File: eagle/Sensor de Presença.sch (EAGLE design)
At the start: 4 parts

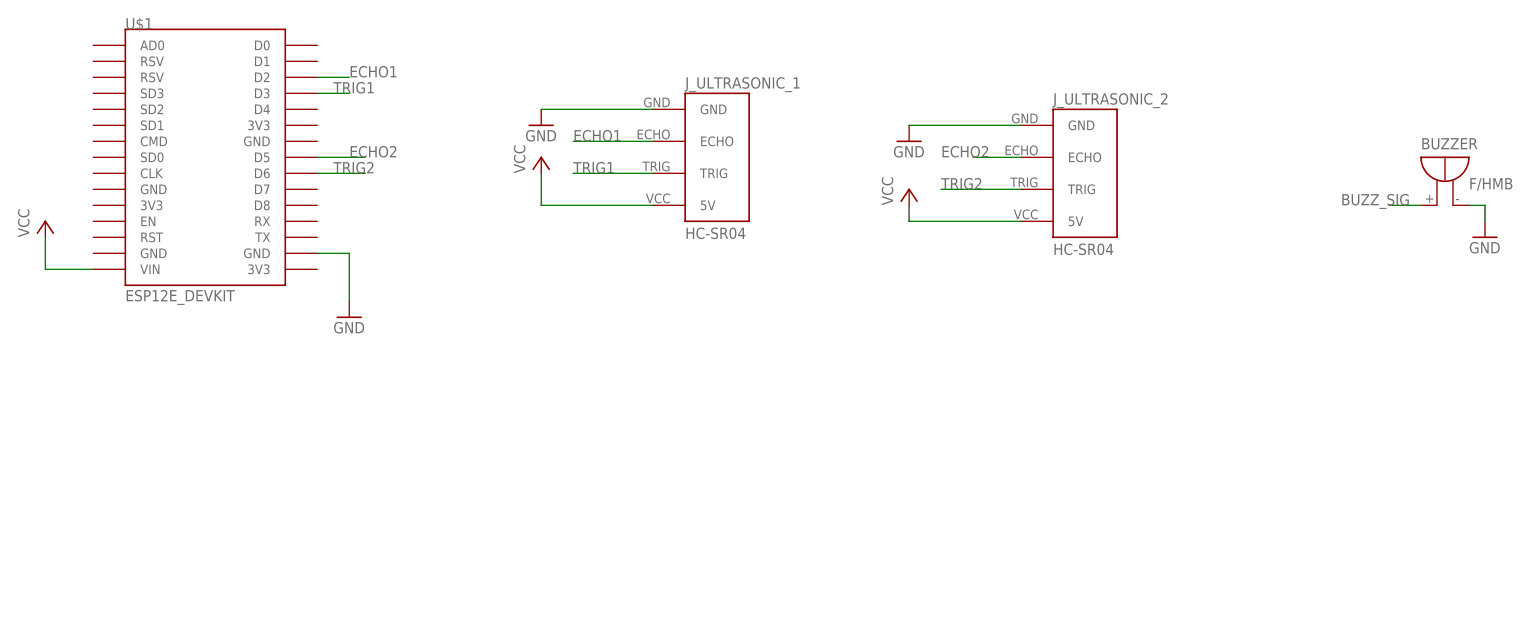
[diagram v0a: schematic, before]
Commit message: updated eagle project to include 2 ultrassonic sensors and ds1307 rtc
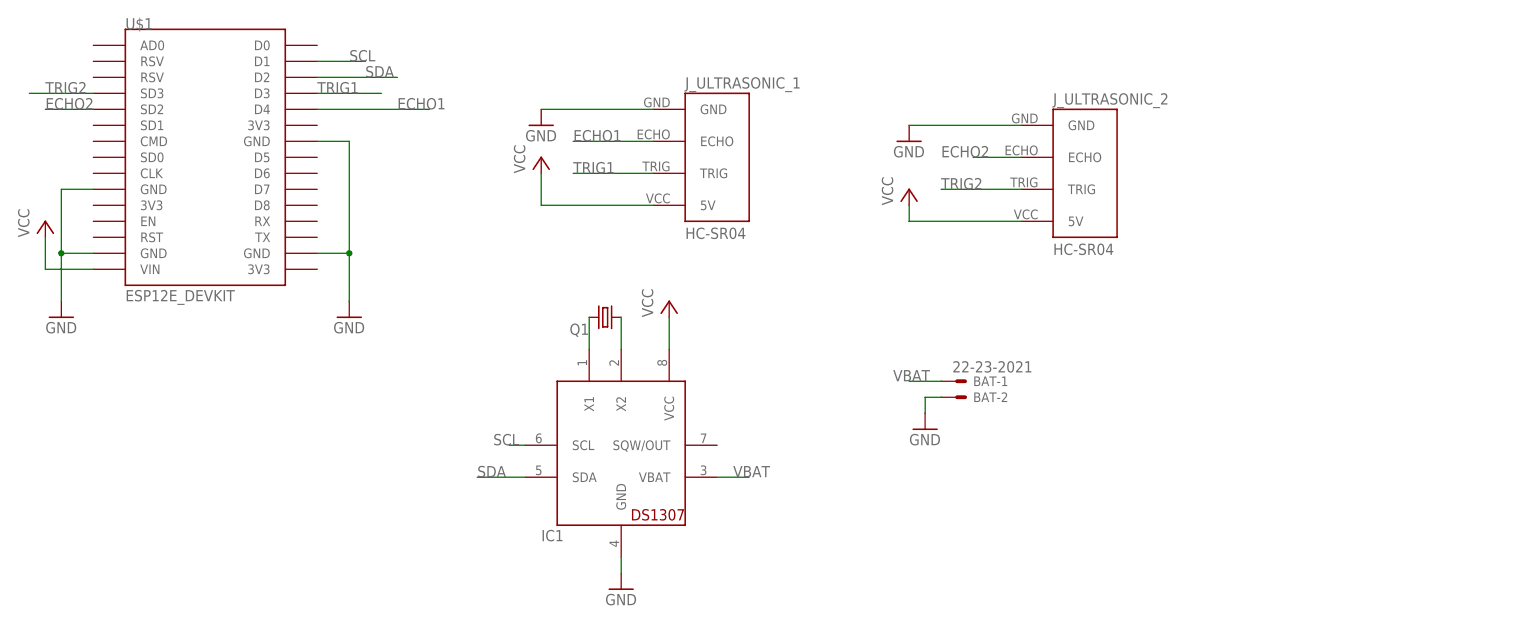
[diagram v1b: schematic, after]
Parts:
- removed BUZZER: F/HMB, buzzer:F/HMB
- added BAT: 22-23-2021, con-molex:22-23-2021
- added IC1: DS1307, adafruit:DS1307
- added Q1: (no value), adafruit:CRYSTALTC38H
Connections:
- removed net BUZZ_SIG: BUZZER.+
- new net N$1: IC1.X1, Q1.2
- new net N$2: IC1.X2, Q1.1
- new net SCL: IC1.SCL, U$1.D1
- new net SDA: IC1.SDA, U$1.D2
- new net VBAT: BAT-1.S, IC1.VBAT
- net ECHO1: now also U$1.D4; no longer U$1.D2
- net ECHO2: now also U$1.SD2; no longer U$1.D5
- net GND: now also BAT-2.S, IC1.GND, U$1.GND@0, U$1.GND@1, U$1.GND@2; no longer BUZZER.-
- net TRIG2: now also U$1.SD3; no longer U$1.D6
- net VCC: now also IC1.VCC

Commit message: added final prototype pcb layout and text
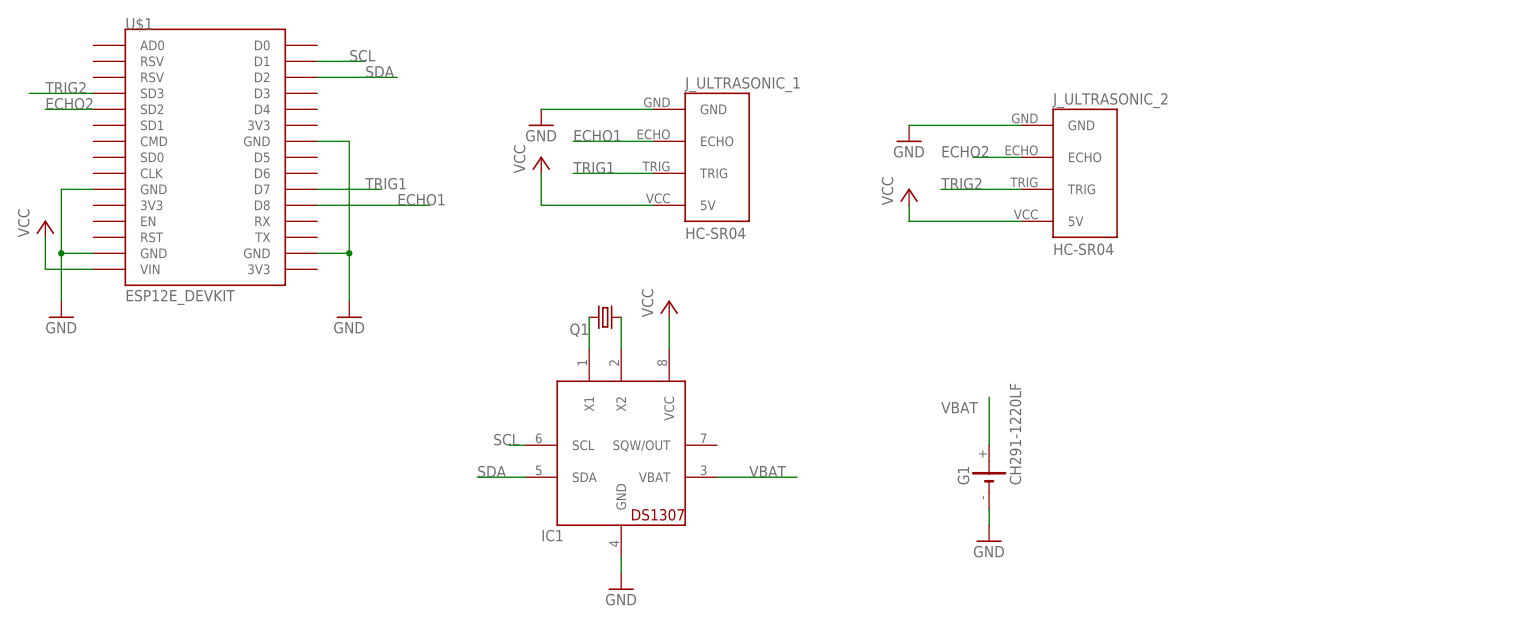
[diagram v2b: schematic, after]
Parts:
- removed BAT: 22-23-2021, con-molex:22-23-2021
- added G1: CH291-1220LF, battery:CH291-1220LF
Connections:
- net ECHO1: now also U$1.D8; no longer U$1.D4
- net GND: now also G1.-; no longer BAT-2.S
- net TRIG1: now also U$1.D7; no longer U$1.D3
- net VBAT: now also G1.+; no longer BAT-1.S
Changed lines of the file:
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@@
 <part name="P+4" library="supply1" library_urn="urn:adsk.eagle:library:371" deviceset="VCC" device=""/>
 <part name="GND4" library="supply1" library_urn="urn:adsk.eagle:library:371" deviceset="GND" device=""/>
-<part name="BAT" library="con-molex" library_urn="urn:adsk.eagle:library:165" deviceset="22-23-2021" device=""/>
 <part name="GND5" library="supply1" library_urn="urn:adsk.eagle:library:371" deviceset="GND" device=""/>
 <part name="Q1" library="adafruit" library_urn="urn:adsk.eagle:library:420" deviceset="CRYSTAL" device="TC38H"/>
 <part name="GND6" library="supply1" library_urn="urn:adsk.eagle:library:371" deviceset="GND" device=""/>
+<part name="G1" library="battery" library_urn="urn:adsk.eagle:library:109" deviceset="CH291-1220LF" device=""/>
 </parts>
 <sheets>
@@
 <instance part="P+4" gate="VCC" x="109.22" y="129.54"/>
 <instance part="GND4" gate="1" x="101.6" y="83.82"/>
-<instance part="BAT" gate="-1" x="154.94" y="116.84"/>
-<instance part="BAT" gate="-2" x="154.94" y="114.3"/>
-<instance part="GND5" gate="1" x="149.86" y="109.22"/>
+<instance part="GND5" gate="1" x="160.02" y="91.44"/>
 <instance part="Q1" gate="G$1" x="99.06" y="127" rot="R180"/>
 <instance part="GND6" gate="1" x="12.7" y="127"/>
+<instance part="G1" gate="G1" x="160.02" y="101.6" rot="R90"/>
 </instances>
 <busses>
@@
 </segment>
 <segment>
-<pinref part="BAT" gate="-2" pin="S"/>
-<wire x1="152.4" y1="114.3" x2="149.86" y2="114.3" width="0.1524" layer="91"/>
-<pinref part="GND5" gate="1" pin="GND"/>
-<wire x1="149.86" y1="114.3" x2="149.86" y2="111.76" width="0.1524" layer="91"/>
-</segment>
-<segment>
 <pinref part="U$1" gate="G$1" pin="GND@1"/>
 <wire x1="17.78" y1="137.16" x2="12.7" y2="137.16" width="0.1524" layer="91"/>
@@
 <junction x="12.7" y="137.16"/>
 </segment>
+<segment>
+<pinref part="GND5" gate="1" pin="GND"/>
+<pinref part="G1" gate="G1" pin="-"/>
+<wire x1="160.02" y1="93.98" x2="160.02" y2="96.52" width="0.1524" layer="91"/>
+</segment>
 </net>
 <net name="ECHO1" class="0">
@@
 </segment>
 <segment>
-<pinref part="U$1" gate="G$1" pin="D4"/>
-<wire x1="53.34" y1="160.02" x2="71.12" y2="160.02" width="0.1524" layer="91"/>
-<label x="66.04" y="160.02" size="1.778" layer="95"/>
+<pinref part="U$1" gate="G$1" pin="D8"/>
+<wire x1="53.34" y1="144.78" x2="71.12" y2="144.78" width="0.1524" layer="91"/>
+<label x="66.04" y="144.78" size="1.778" layer="95"/>
 </segment>
 </net>
@@
 </segment>
 <segment>
-<pinref part="U$1" gate="G$1" pin="D3"/>
-<wire x1="53.34" y1="162.56" x2="63.5" y2="162.56" width="0.1524" layer="91"/>
-<label x="53.34" y="162.56" size="1.778" layer="95"/>
+<pinref part="U$1" gate="G$1" pin="D7"/>
+<wire x1="53.34" y1="147.32" x2="63.5" y2="147.32" width="0.1524" layer="91"/>
+<label x="60.96" y="147.32" size="1.778" layer="95"/>
 </segment>
 </net>
@@
 </segment>
 </net>
-<net name="VBAT" class="0">
-<segment>
-<pinref part="BAT" gate="-1" pin="S"/>
-<wire x1="152.4" y1="116.84" x2="147.32" y2="116.84" width="0.1524" layer="91"/>
-<label x="144.78" y="116.84" size="1.778" layer="95"/>
-</segment>
-<segment>
-<pinref part="IC1" gate="G$1" pin="VBAT"/>
-<wire x1="116.84" y1="101.6" x2="121.92" y2="101.6" width="0.1524" layer="91"/>
-<label x="119.38" y="101.6" size="1.778" layer="95"/>
-</segment>
-</net>
 <net name="N$1" class="0">
 <segment>
@@
 </segment>
 </net>
+<net name="VBAT" class="0">
+<segment>
+<pinref part="IC1" gate="G$1" pin="VBAT"/>
+<wire x1="116.84" y1="101.6" x2="129.54" y2="101.6" width="0.1524" layer="91"/>
+<label x="121.92" y="101.6" size="1.778" layer="95"/>
+</segment>
+<segment>
+<pinref part="G1" gate="G1" pin="+"/>
+<wire x1="160.02" y1="106.68" x2="160.02" y2="114.3" width="0.1524" layer="91"/>
+<label x="152.4" y="111.76" size="1.778" layer="95"/>
+</segment>
+</net>
